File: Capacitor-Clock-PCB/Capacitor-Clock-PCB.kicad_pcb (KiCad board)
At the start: 2 copper layers, 87 x 75 mm, 54 parts, among them J1 Conn_01x04, J2 Jack-DC, J3 Conn_01x02, J4 Conn_01x02, J5 Conn_01x05, J6 Conn_01x05, J7 Conn_01x04_Socket, J8 Conn_01x02, U1 AP63205WU, U3 ULN2003A, U4 AP63203WU, U5 MP6002DN-LF-Z

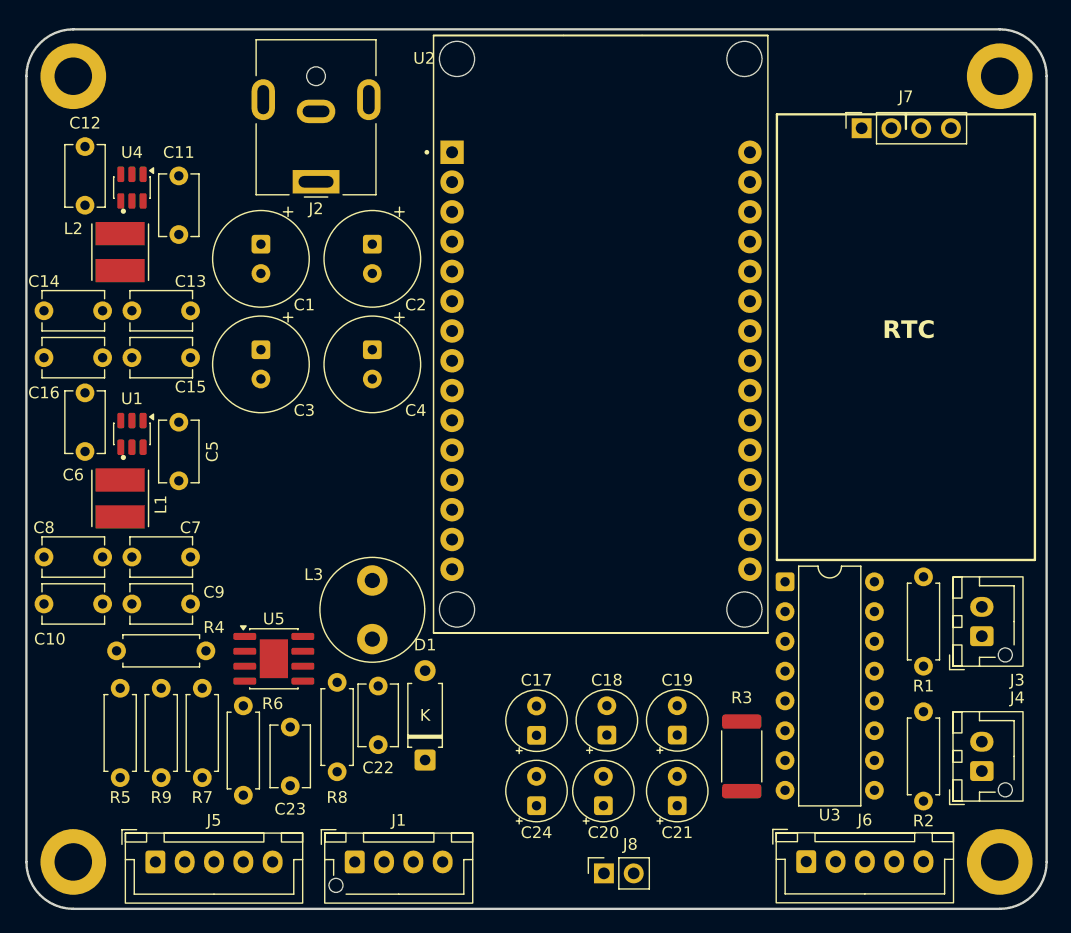
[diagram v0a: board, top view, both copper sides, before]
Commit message: finished preliminary routing
finished routing ready for review
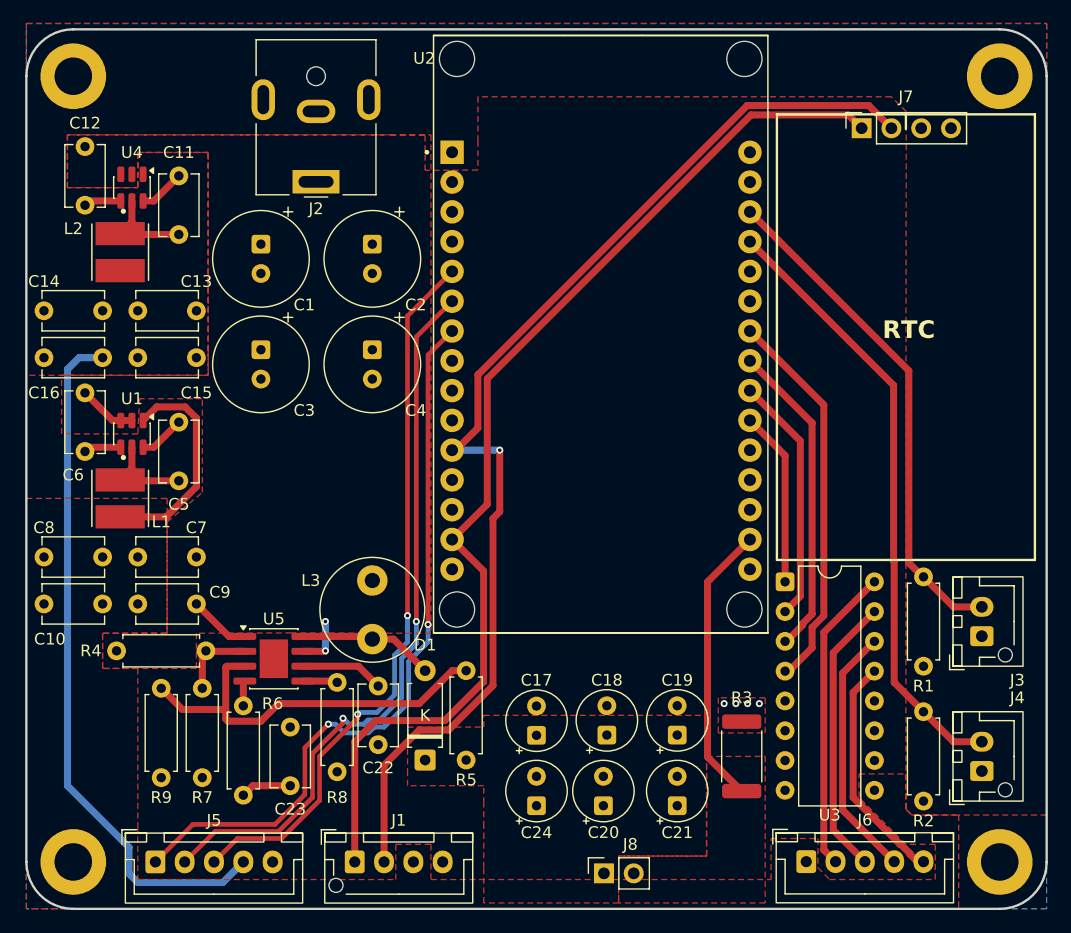
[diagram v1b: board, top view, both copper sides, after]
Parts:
- moved R5 29.5 mm to (100.5, 112.3)
- moved C15 5.50 mm to (77.5, 78.0), turned to 180 degrees
- moved C13 0.50 mm to (77.5, 74.0)
- moved C7 0.50 mm to (77.5, 95.0)
- moved C9 0.50 mm to (77.5, 99.0)
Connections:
- U1 pad 2: Net-(U1-EN) -> +12V
- U2 pad 12: unconnected-(U2-G12-Pad12) -> /Button2
- U2 pad 13: unconnected-(U2-G13-Pad13) -> /Button1
- U2 pad 21: /Button1 -> unconnected-(U2-G19-Pad21)
- U2 pad 22: /Button2 -> unconnected-(U2-G18-Pad22)
- U4 pad 2: Net-(U1-EN) -> +12V
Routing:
- net /SDA: track 0.00 -> 97.8 mm, vias 0 -> 1
- net /SCL: track 0.00 -> 93.3 mm
- net /SW: track 0.00 -> 63.4 mm, vias 0 -> 2
- net /DT: track 0.00 -> 62.7 mm, vias 0 -> 2
- net /CLK: track 0.00 -> 61.8 mm, vias 0 -> 2
- net +3V3: track 0.00 -> 59.4 mm
- net /Button2: track 0.00 -> 52.3 mm
- net /Button1: track 0.00 -> 43.3 mm
- net Net-(U5-FB): track 0.00 -> 34.7 mm
- net /Step4: track 0.00 -> 33.2 mm
- net /Step3: track 0.00 -> 27.1 mm
- net Net-(J6-Pin_2): track 0.00 -> 26.1 mm
- net /I_sense: track 0.00 -> 24.2 mm
- net Net-(J6-Pin_3): track 0.00 -> 23.9 mm
- net Net-(J6-Pin_4): track 0.00 -> 21.7 mm
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- added copper zone on F.Cu, net +12V
- added copper zone on F.Cu, net +3V3
- added copper zone on F.Cu, net +5V
- added copper zone on F.Cu, net /+19V
- added copper zone on F.Cu, net /I_sense
- added copper zone on B.Cu, net GND
- added copper zone on F.Cu, net GND

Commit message: Update post  design review
updated schematic and pcb with notes from review. added switchable fan header, ability to control output prongs, and RGB header
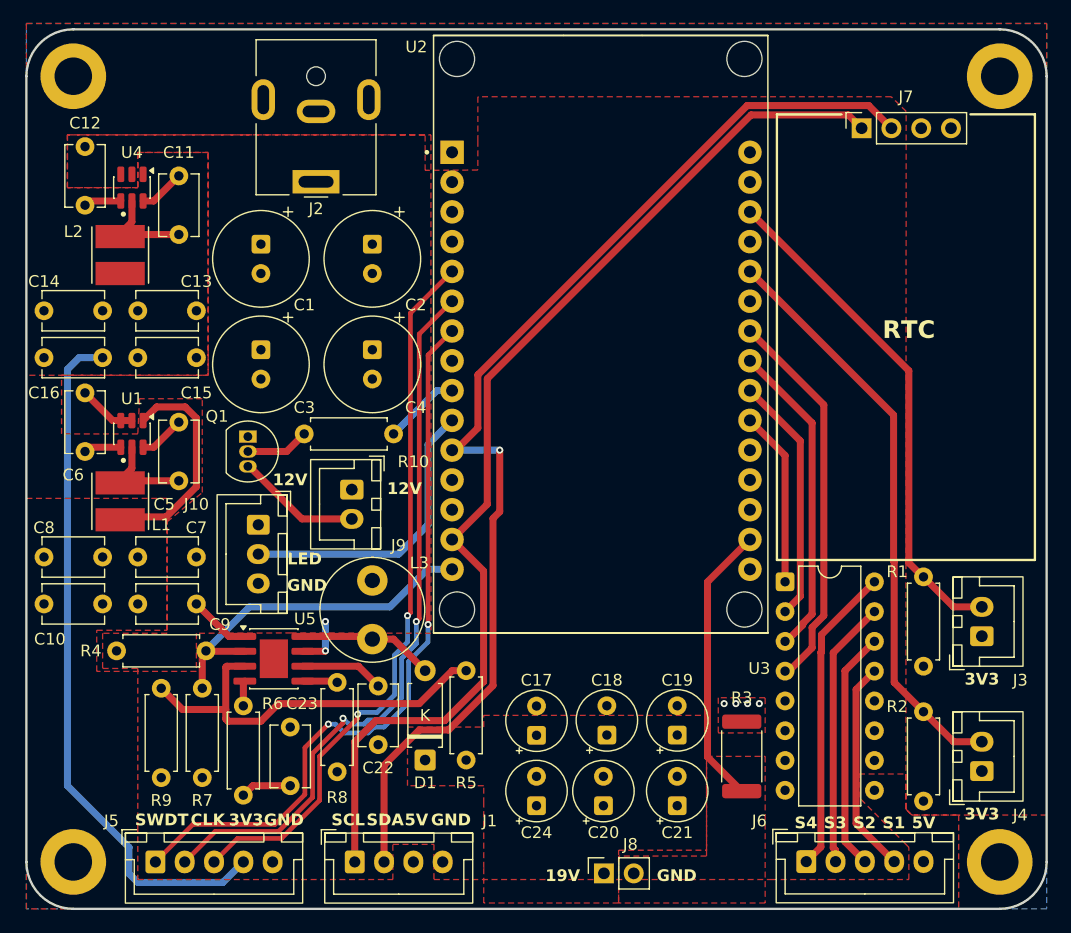
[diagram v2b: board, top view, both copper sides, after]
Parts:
- added J10: Conn_01x03, Connector_JST:JST_XH_B3B-XH-A_1x03_P2.50mm_Vertical, F.Cu at (82.8, 92.2)
- added J9: Conn_01x02, Connector_JST:JST_XH_B2B-XH-A_1x02_P2.50mm_Vertical, F.Cu at (90.8, 89.2)
- added Q1: 2N3904, Package_TO_SOT_THT:TO-92_Inline, F.Cu at (81.9, 84.7)
- added R10: 330, Resistor_THT:R_Axial_DIN0207_L6.3mm_D2.5mm_P7.62mm_Horizontal, F.Cu at (94.3, 84.5)
- J1: footprint Connector_JST:JST_XH_B4B-XH-AM_1x04_P2.50mm_Vertical -> Connector_JST:JST_XH_B4B-XH-A_1x04_P2.50mm_Vertical
- J3, J4: footprint Connector_JST:JST_XH_B2B-XH-AM_1x02_P2.50mm_Vertical -> Connector_JST:JST_XH_B2B-XH-A_1x02_P2.50mm_Vertical
- moved L1 0.25 mm to (71.0, 90.2)
- moved L2 0.25 mm to (71.0, 69.2)
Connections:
- J6 pad 1: +5V -> Net-(J6-Pin_1)
- J6 pad 5: Net-(J6-Pin_5) -> +5V
- R4 pad 2: Net-(U5-LINE) -> /LINE
- R7 pad 1: Net-(U5-LINE) -> /LINE
- U2 pad 11: unconnected-(U2-G14-Pad11) -> /Button2
- U2 pad 12: /Button2 -> unconnected-(U2-G12-Pad12)
- U2 pad 16: unconnected-(U2-G23-Pad16) -> /LINE
- U2 pad 21: unconnected-(U2-G19-Pad21) -> /LED
- U2 pad 22: unconnected-(U2-G18-Pad22) -> /Fan Control
- U3 pad 13: Net-(J6-Pin_5) -> Net-(J6-Pin_4)
- U3 pad 14: Net-(J6-Pin_4) -> Net-(J6-Pin_3)
- U3 pad 15: Net-(J6-Pin_3) -> Net-(J6-Pin_2)
- U3 pad 16: Net-(J6-Pin_2) -> Net-(J6-Pin_1)
- U5 pad 2: Net-(U5-LINE) -> /LINE
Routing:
- net /LINE: track 0.00 -> 30.5 mm
- net Net-(J6-Pin_1): track 0.00 -> 26.3 mm
- net /LED: track 0.00 -> 25.3 mm
- net Net-(J6-Pin_5): track 19.8 -> 0.00 mm
- net Net-(J9-Pin_2): track 0.00 -> 10.7 mm
- net Net-(U5-LINE): track 6.65 -> 0.00 mm
- net /Fan Control: track 0.00 -> 6.52 mm
- net Net-(Q1-B): track 0.00 -> 5.42 mm
- net Net-(J6-Pin_4): track 21.7 -> 18.2 mm
- net Net-(J6-Pin_3): track 23.9 -> 20.5 mm
- net Net-(J6-Pin_2): track 26.1 -> 22.9 mm
- net /Button2: track 52.3 -> 49.7 mm
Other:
- board text added: "12V"
- board text added: "19V"
- board text added: "3V3"
- board text added: "5V"
- board text added: "CLK"
- board text added: "DT"
- board text added: "GND"
- board text added: "LED"
- board text added: "S1"
- board text added: "S2"
- board text added: "S3"
- board text added: "S4"
- board text added: "SCL"
- board text added: "SDA"
- board text added: "SW"
